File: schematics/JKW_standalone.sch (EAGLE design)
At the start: 165 parts, among them IC1 4093D, IC2 AT-MEGA-8, IC4 ATMEGA2560-16AU, T1 Farnell: 1299313, T2 Farnell: 1299313, T3 Farnell: 1299313, T4 T-IRLMS6702, T5 Farnell: 1299313

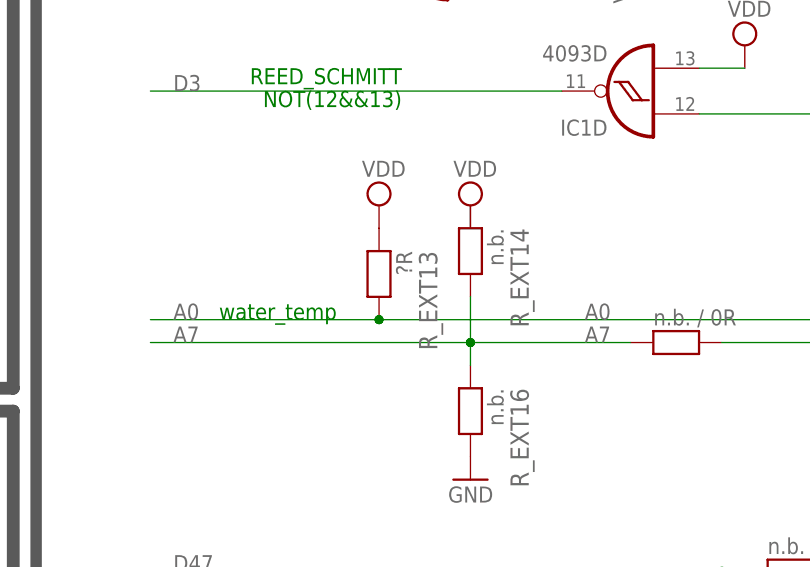
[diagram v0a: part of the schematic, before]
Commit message: Water compare resistor added
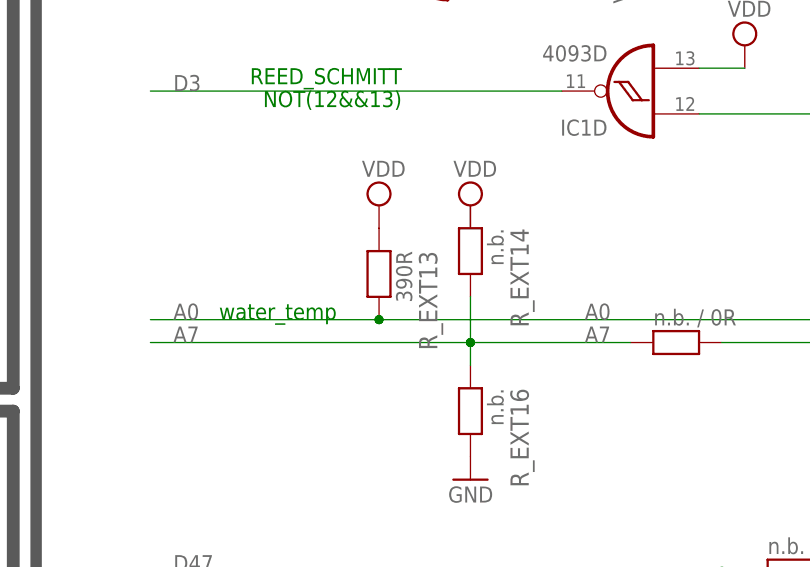
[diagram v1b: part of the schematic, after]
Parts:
- R_EXT13: value ?R -> 390R
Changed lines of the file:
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@@
 <part name="SUPPLY12" library="supply2" deviceset="VDD" device=""/>
 <part name="SUPPLY16" library="supply2" deviceset="VDD" device=""/>
-<part name="R_EXT13" library="RCLDT" deviceset="R" device="0805" value="?R"/>
+<part name="R_EXT13" library="RCLDT" deviceset="R" device="0805" value="390R"/>
 <part name="R_EXT14" library="RCLDT" deviceset="R" device="0805" value="n.b."/>
 <part name="R_EXT16" library="RCLDT" deviceset="R" device="0805" value="n.b."/>

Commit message: New plug
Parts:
- removed ST3, ST4: (no value), Stift+Buchsenleisten:BU_1X4_BL17-SMD
- D7: value SS24 -> n.b. / 20V-ZD.; device RCLDT:D-SSMB-A+K -> diode:ZENER-DIODESOD80C
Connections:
- removed net A10: IC4.PK2(ADC10/PCINT18)
- removed net D20: IC4.(SDA/INT1)PD1, R_SDA_UP.2, ST3.2
- removed net D21: IC4.(SCL/INT0)PD0, R_SCL_UP.2, ST3.3
- removed net EXT_3.3V: C9.1, R_TEMP_ALERT.2, ST4.4, TMP102AIDRLT.ADD0, TMP102AIDRLT.VCC
- removed net EXT_GND: C9.2, ST4.1, TMP102AIDRLT.GND
- removed net EXT_SCL: ST4.2, TMP102AIDRLT.SCL
- removed net EXT_SDA: ST4.3, TMP102AIDRLT.SDA
- new net SCL: IC4.(SCL/INT0)PD0, R_SCL_UP.2, TMP102AIDRLT.SCL
- new net SDA: IC4.(SDA/INT1)PD1, R_SDA_UP.2, TMP102AIDRLT.SDA
- net +3V3_EXT: now also C9.1, R_TEMP_ALERT.2, TMP102AIDRLT.ADD0, TMP102AIDRLT.VCC; no longer ST3.1
- net GND: now also C9.2, TMP102AIDRLT.GND; no longer ST3.4
- net KUPPLUNG_IN: now also D7.C; no longer D7.K
- net V_BAK: now also IC4.PK2(ADC10/PCINT18)
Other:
- note added: "GPS Bat (A10)"

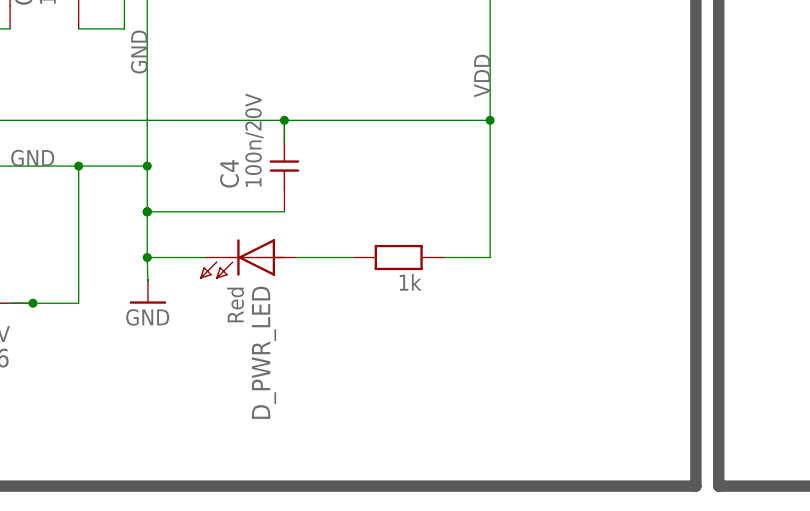
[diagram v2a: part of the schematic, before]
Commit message: GPS surrounded by GND
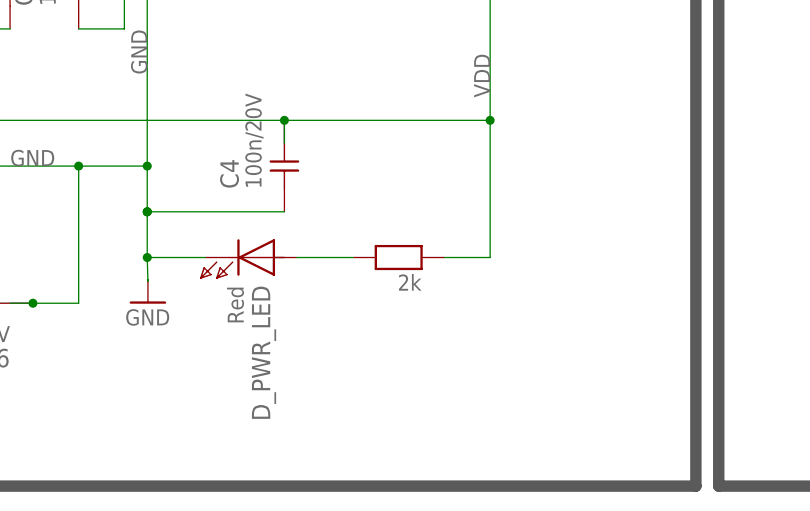
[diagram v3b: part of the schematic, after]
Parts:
- R_LED_5V: value 1k -> 2k
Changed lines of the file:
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@@
 <part name="R38" library="RCLDT" deviceset="R" device="0805" value="n.b."/>
 <part name="R39" library="RCLDT" deviceset="R" device="0805" value="n.b."/>
-<part name="R_LED_5V" library="RCLDT" deviceset="R" device="0805" value="1k"/>
+<part name="R_LED_5V" library="RCLDT" deviceset="R" device="0805" value="2k"/>
 <part name="R_SCL_UP" library="RCLDT" deviceset="R" device="0805" value="1K"/>
 <part name="R_SDA_UP" library="RCLDT" deviceset="R" device="0805" value="1K"/>

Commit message: added 3V emergency voltage
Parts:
- added D13, D14: (no value), semicon-smd-ipc:D-A1-C3
- added D15: Mouser 863-NSR1020MW2T3G, diode:DIODE-SOD323-W
- added D16: n.b. / 20V-ZD., diode:ZENER-DIODESOT23
- D1, D2, D6, D8: device diode:ZENER-DIODESOD80C -> diode:ZENER-DIODESOT23
- D18, D19: value n.b. / 20V-ZD. -> 78-MMBZ5232B-V; device diode:ZENER-DIODESOD80C -> diode:ZENER-DIODESOT23
- D7: value n.b. / 20V-ZD. -> 771-PMBD7000235; device diode:ZENER-DIODESOD80C -> semicon-smd-ipc:D-A1-C3
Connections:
- removed net V_BAK: BAT_CLIP1.+, C7.1, GPS.VBACKUP, IC4.PK2(ADC10/PCINT18)
- new net A10: C7.1, D14.C, D15.C, GPS.VBACKUP, IC4.PK2(ADC10/PCINT18)
- new net N$11: BAT_CLIP1.+, D15.A
- new net N$47: D13.C, D14.A
- net D24: now also D13.A
- net D48: now also D16.C
- net GND: now also D16.A
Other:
- note added: "GPS_V_BACKUP"
- moved on the sheet: C7
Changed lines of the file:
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@@
 <part name="GND9" library="SparkFun" deviceset="GND" device=""/>
 <part name="DCDC53.3" library="Kolja" deviceset="AP1117E33G" device=""/>
-<part name="D6" library="diode" deviceset="ZENER-DIODE" device="SOD80C" value="20V-Zdiode"/>
+<part name="D6" library="diode" deviceset="ZENER-DIODE" device="SOT23" value="20V-Zdiode"/>
 <part name="GND12" library="SparkFun" deviceset="GND" device=""/>
 <part name="GND14" library="SparkFun" deviceset="GND" device=""/>
@@
 <part name="D17" library="RCLDT" deviceset="D-S" device="SMB-A+K" value="SS24"/>
 <part name="12V_F1" library="Kolja" deviceset="POLY_FUSE" device="" value="1.1A"/>
-<part name="D18" library="diode" deviceset="ZENER-DIODE" device="SOD80C" value="n.b. / 20V-ZD."/>
-<part name="D19" library="diode" deviceset="ZENER-DIODE" device="SOD80C" value="n.b. / 20V-ZD."/>
+<part name="D18" library="diode" deviceset="ZENER-DIODE" device="SOT23" value="78-MMBZ5232B-V"/>
+<part name="D19" library="diode" deviceset="ZENER-DIODE" device="SOT23" value="78-MMBZ5232B-V"/>
 <part name="GND6" library="supply1" deviceset="GND" device=""/>
 <part name="GND15" library="supply1" deviceset="GND" device=""/>
@@
 <part name="R_EXT12" library="RCLDT" deviceset="R" device="0805" value="5k"/>
 <part name="GND17" library="supply1" deviceset="GND" device=""/>
-<part name="D1" library="diode" deviceset="ZENER-DIODE" device="SOD80C" value="5.5V"/>
-<part name="D2" library="diode" deviceset="ZENER-DIODE" device="SOD80C" value="5.5V"/>
-<part name="D8" library="diode" deviceset="ZENER-DIODE" device="SOD80C" value="5.5V"/>
+<part name="D1" library="diode" deviceset="ZENER-DIODE" device="SOT23" value="5.5V"/>
+<part name="D2" library="diode" deviceset="ZENER-DIODE" device="SOT23" value="5.5V"/>
+<part name="D8" library="diode" deviceset="ZENER-DIODE" device="SOT23" value="5.5V"/>
 <part name="D9" library="diode" deviceset="ZENER-DIODE" device="SOD80C" value="5.5V"/>
 <part name="D12" library="diode" deviceset="ZENER-DIODE" device="SOD80C" value="20V"/>
@@
 <part name="SUPPLY8" library="supply2" deviceset="VDD" device=""/>
 <part name="SUPPLY19" library="supply2" deviceset="VDD" device=""/>
-<part name="D7" library="diode" deviceset="ZENER-DIODE" device="SOD80C" value="n.b. / 20V-ZD."/>
+<part name="D7" library="semicon-smd-ipc" deviceset="D-" device="A1-C3" value="771-PMBD7000235"/>
+<part name="D13" library="semicon-smd-ipc" deviceset="D-" device="A1-C3"/>
+<part name="D14" library="semicon-smd-ipc" deviceset="D-" device="A1-C3"/>
+<part name="D15" library="diode" deviceset="DIODE-" device="SOD323-W" value="Mouser 863-NSR1020MW2T3G"/>
+<part name="D16" library="diode" deviceset="ZENER-DIODE" device="SOT23" value="n.b. / 20V-ZD."/>
+<part name="U$2" library="SUPPLY" deviceset="GND" device=""/>
 </parts>
 <sheets>
@@
 <text x="35.56" y="139.7" size="1.778" layer="91">water_temp</text>
 <text x="-266.7" y="139.7" size="1.778" layer="91">GPS Bat (A10)</text>
+<text x="-142.24" y="226.06" size="1.778" layer="91">GPS_V_BACKUP</text>
 </plain>
 <instances>
@@
 <attribute name="VALUE" x="271.78" y="106.68" size="1.778" layer="96"/>
 </instance>
-<instance part="C7" gate="C" x="236.22" y="86.36"/>
+<instance part="C7" gate="C" x="236.22" y="93.98"/>
 <instance part="D_GPS_FIX" gate="G$1" x="279.4" y="86.36" smashed="yes" rot="R90">
 <attribute name="NAME" x="277.4061" y="89.0016" size="1.6764" layer="95"/>
@@
 <attribute name="VALUE" x="137.922" y="169.291" size="1.778" layer="96"/>
 </instance>
+<instance part="D13" gate="G$1" x="254" y="119.38"/>
+<instance part="D14" gate="G$1" x="261.62" y="119.38"/>
+<instance part="D15" gate="G$1" x="231.14" y="86.36" rot="R90"/>
+<instance part="D16" gate="G$1" x="127" y="172.72" smashed="yes" rot="R90">
+<attribute name="NAME" x="125.095" y="170.942" size="1.778" layer="95" rot="R90"/>
+<attribute name="VALUE" x="130.429" y="160.782" size="1.778" layer="96" rot="R90"/>
+</instance>
+<instance part="U$2" gate="G$1" x="127" y="165.1"/>
 </instances>
 <busses>
@@
 <wire x1="287.02" y1="83.82" x2="254" y2="83.82" width="0.1524" layer="91"/>
 <wire x1="254" y1="83.82" x2="241.3" y2="83.82" width="0.1524" layer="91"/>
-<wire x1="241.3" y1="83.82" x2="241.3" y2="86.36" width="0.1524" layer="91"/>
-<wire x1="241.3" y1="86.36" x2="241.3" y2="104.14" width="0.1524" layer="91"/>
+<wire x1="241.3" y1="83.82" x2="241.3" y2="93.98" width="0.1524" layer="91"/>
+<wire x1="241.3" y1="93.98" x2="241.3" y2="104.14" width="0.1524" layer="91"/>
 <wire x1="241.3" y1="78.74" x2="241.3" y2="83.82" width="0.1524" layer="91"/>
 <wire x1="287.02" y1="83.82" x2="287.02" y2="86.36" width="0.1524" layer="91"/>
@@
 <junction x="241.3" y="83.82"/>
 <junction x="269.24" y="104.14"/>
-<junction x="241.3" y="86.36"/>
+<junction x="241.3" y="93.98"/>
 <junction x="287.02" y="83.82"/>
 <junction x="254" y="73.66"/>
@@
 <wire x1="289.24" y1="228.6" x2="294.32" y2="228.6" width="0.1524" layer="91"/>
 </segment>
+<segment>
+<pinref part="D16" gate="G$1" pin="A"/>
+<pinref part="U$2" gate="G$1" pin="GND"/>
+<wire x1="127" y1="170.18" x2="127" y2="167.64" width="0.1524" layer="91"/>
+</segment>
 </net>
 <net name="DZ" class="0">
@@
 <segment>
 <pinref part="U$1" gate="G$1" pin="MC_COI"/>
-<wire x1="185.42" y1="177.8" x2="132.08" y2="177.8" width="0.1524" layer="91"/>
+<wire x1="185.42" y1="177.8" x2="127" y2="177.8" width="0.1524" layer="91"/>
 <label x="139.7" y="177.8" size="1.778" layer="95"/>
+<pinref part="D16" gate="G$1" pin="C"/>
+<wire x1="127" y1="177.8" x2="119.38" y2="177.8" width="0.1524" layer="91"/>
+<wire x1="127" y1="175.26" x2="127" y2="177.8" width="0.1524" layer="91"/>
+<junction x="127" y="177.8"/>
 </segment>
 </net>
@@
 <pinref part="IC4" gate="1" pin="(AD2)PA2"/>
 </segment>
+<segment>
+<pinref part="D13" gate="G$1" pin="A"/>
+<wire x1="251.46" y1="119.38" x2="241.3" y2="119.38" width="0.1524" layer="91"/>
+<label x="241.3" y="119.38" size="1.778" layer="95"/>
+</segment>
 </net>
 <net name="D25" class="0">
@@
 </segment>
 </net>
-<net name="V_BAK" class="0">
-<segment>
-<wire x1="231.14" y1="96.52" x2="281.94" y2="96.52" width="0.1524" layer="91"/>
-<wire x1="281.94" y1="96.52" x2="281.94" y2="93.98" width="0.1524" layer="91"/>
-<wire x1="281.94" y1="93.98" x2="292.1" y2="93.98" width="0.1524" layer="91"/>
-<wire x1="231.14" y1="78.74" x2="231.14" y2="86.36" width="0.1524" layer="91"/>
-<wire x1="231.14" y1="86.36" x2="231.14" y2="96.52" width="0.1524" layer="91"/>
-<junction x="231.14" y="86.36"/>
-<label x="246.38" y="83.82" size="1.778" layer="95" rot="R90"/>
-<pinref part="GPS" gate="G$1" pin="VBACKUP"/>
-<pinref part="BAT_CLIP1" gate="G$1" pin="+"/>
-<pinref part="C7" gate="C" pin="1"/>
-</segment>
-<segment>
-<wire x1="-228.6" y1="139.7" x2="-246.38" y2="139.7" width="0.1524" layer="91"/>
-<label x="-243.84" y="139.7" size="1.778" layer="95"/>
-<pinref part="IC4" gate="1" pin="PK2(ADC10/PCINT18)"/>
-</segment>
-</net>
 <net name="N$15" class="0">
 <segment>
@@
 <wire x1="251.46" y1="60.96" x2="251.46" y2="66.04" width="0.1524" layer="91"/>
 <junction x="251.46" y="66.04"/>
-<label x="279.4" y="78.74" size="1.778" layer="95"/>
+<label x="269.24" y="78.74" size="1.778" layer="95"/>
 <pinref part="GPS" gate="G$1" pin="RXD"/>
 <pinref part="R40" gate="G$1" pin="1"/>
@@
 </segment>
 </net>
+<net name="N$47" class="0">
+<segment>
+<pinref part="D14" gate="G$1" pin="A"/>
+<pinref part="D13" gate="G$1" pin="C"/>
+<wire x1="259.08" y1="119.38" x2="256.54" y2="119.38" width="0.1524" layer="91"/>
+</segment>
+</net>
+<net name="A10" class="0">
+<segment>
+<wire x1="-228.6" y1="139.7" x2="-246.38" y2="139.7" width="0.1524" layer="91"/>
+<label x="-233.68" y="139.7" size="1.778" layer="95"/>
+<pinref part="IC4" gate="1" pin="PK2(ADC10/PCINT18)"/>
+</segment>
+<segment>
+<pinref part="GPS" gate="G$1" pin="VBACKUP"/>
+<wire x1="281.94" y1="96.52" x2="281.94" y2="93.98" width="0.1524" layer="91"/>
+<wire x1="281.94" y1="93.98" x2="292.1" y2="93.98" width="0.1524" layer="91"/>
+<wire x1="266.7" y1="96.52" x2="281.94" y2="96.52" width="0.1524" layer="91"/>
+<wire x1="266.7" y1="96.52" x2="266.7" y2="119.38" width="0.1524" layer="91"/>
+<pinref part="D14" gate="G$1" pin="C"/>
+<wire x1="266.7" y1="119.38" x2="264.16" y2="119.38" width="0.1524" layer="91"/>
+<junction x="266.7" y="119.38"/>
+<wire x1="266.7" y1="119.38" x2="281.94" y2="119.38" width="0.1524" layer="91"/>
+<label x="274.32" y="119.38" size="1.778" layer="95"/>
+<pinref part="C7" gate="C" pin="1"/>
+<wire x1="266.7" y1="96.52" x2="231.14" y2="96.52" width="0.1524" layer="91"/>
+<wire x1="231.14" y1="96.52" x2="231.14" y2="93.98" width="0.1524" layer="91"/>
+<pinref part="D15" gate="G$1" pin="C"/>
+<wire x1="231.14" y1="88.9" x2="231.14" y2="93.98" width="0.1524" layer="91"/>
+<junction x="231.14" y="93.98"/>
+</segment>
+</net>
+<net name="N$11" class="0">
+<segment>
+<pinref part="D15" gate="G$1" pin="A"/>
+<pinref part="BAT_CLIP1" gate="G$1" pin="+"/>
+<wire x1="231.14" y1="83.82" x2="231.14" y2="78.74" width="0.1524" layer="91"/>
+</segment>
+</net>

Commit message: GPS schematic updated
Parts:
- removed R28: 1k, RCLDT:R0805
- removed R40: 2k7, RCLDT:R0805
- removed R41: 1k2, RCLDT:R0805
- removed R_OIL_V_DIV_2: 220, RCLDT:R0805
- added D20: 5.5V, diode:ZENER-DIODESOT23
- added R_GPS_LED: 1k, RCLDT:R0805
- added R_OIL_UP: 220, RCLDT:R0805
- added R_TX_DOWN: 2k7, RCLDT:R0805
- added R_TX_UP: 1k2, RCLDT:R0805
- S6: value U -> Left
- S7: value R -> Down
- S8: value D -> Up
- S9: value L -> Right
- renumbered 18632422 to RGB_3, D10 to D_L1, D11 to D_L2, D3 to D_L0, R1 to R_BL_L, R10 to R_REED_DOWN, R11 to R_REED, R12 to R_R_LED_3, R13 to R_G_LED_3, R14 to R_B_LED_3, R15 to R_L0, R16 to R_L1, R17 to R_L2, R18 to R_R_LED_2, R19 to R_G_LED_2, R2 to R_RES_UP, R20 to R_B_LED_2, R21 to R_R_LED_1, R22 to R_G_LED_1, R23 to R_B_LED_1, R24 to R_R_LED_0, R25 to R_G_LED_0, R26 to R_B_LED_0, R27 to R_N, R29 to R_R_LED_4, R3 to AT8_REF, R30 to R_G_LED_4, R31 to R_B_LED_4, R32 to R_R_LED_5, R33 to R_G_LED_5, R34 to R_B_LED_5, R35 to R_R_LED_6, R36 to R_G_LED_6, R37 to R_B_LED_6, R38 to R_E1_4, R39 to R_E1_2, R4 to R_BL_R, R43 to R_E2_1, R44 to R_E1_3, R45 to R_E0_0, R46 to R_E0_1, R47 to R_E0_3, R48 to R_E0_4, R49 to R_E0_2, R5 to R_OIL, R6 to R_HIGHB, R7 to R_REED_UP, R8 to R_E1_0, R9 to R_E1_1, R_DZ_DIV1 to R_DZ, R_DZ_DIV2 to R_DZ_DOWN, R_EXT10 to R_FLASHR, R_EXT11 to R_HB, R_EXT12 to R_HB_DOWN, R_EXT13 to R_WATER_UP, R_EXT14 to R_E2_0, R_EXT16 to R_E2_2, R_EXT7 to R_FLASHL, R_EXT8 to R_FLASHL_DOWN, R_EXT9 to R_FLASHR_DOWN, U$14 to RGB_7, U$15 to RGB_4, U$16 to RGB_6, U$18 to RGB_5, U$19 to RGB_2, U$20 to RGB_1
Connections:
- net B_D renamed B_UP
- net B_L renamed B_RIGHT
- net B_R renamed B_DOWN
- net B_U renamed B_LEFT
- net D35 renamed DISP_SCL
- net A1: now also D20.C, R_OIL_UP.1; no longer R_OIL_V_DIV_2.1
- net GND: now also D20.A, R_TX_DOWN.2; no longer R40.2
- net N$15: now also R_GPS_LED.2; no longer R28.2
- net N$17: now also R_GPS_LED.1; no longer R28.1
- net TX1: now also R_TX_UP.2; no longer R41.2
- net TX1_3.3: now also R_TX_DOWN.1, R_TX_UP.1; no longer R40.1, R41.1
- net VDD: now also R_OIL_UP.2; no longer R_OIL_V_DIV_2.2
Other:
- note removed: "Floatet das? Warum ist da kein Pullup?"
- note removed: "SpeedSensor"
- note removed: "down"
- note removed: "left"
- note removed: "right"
- note removed: "up"
- moved on the sheet: BAT_CLIP1, C5, C7, D13, D14, D15, D9, D_GPS_FIX, R_V_HIGH, R_V_LOW, S6, S7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

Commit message: Changed to push buttons with plate
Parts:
- removed C38: 2µ2/100V, RCLDT:C0805
- removed C46: 470µ, RCLDT:C-ELKO-5-8X13R
- removed C49: 470µ, RCLDT:C-ELKO-5-8X13
- removed S6: Left, SWITCH+RELAIS:SW-TASTERECO-DIAGONAL
- removed S7: Down, SWITCH+RELAIS:SW-TASTERECO-DIAGONAL
- removed S8: Up, SWITCH+RELAIS:SW-TASTERECO-DIAGONAL
- removed S9: Right, SWITCH+RELAIS:SW-TASTERECO-DIAGONAL
- added B_DOWN, B_LEFT, B_RIGHT, B_UP: SMD_TASTER_MIT_KAPPE, Kolja:SMD_TASTER_MIT_KAPPE
- added CP1, CP2, CP3, CP4: 220µF/16V, Kolja:C_SMD_SMP
- added D10, D21, D22, D3: 5.5V, diode:ZENER-DIODESOT23
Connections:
- removed net D37: IC4.(A8)PC0
- removed net D40: IC4.(RD)PG1
- removed net D41: IC4.(WR)PG0
- net A0: now also D3.C
- net A7: now also D22.C
- net BAT+: now also CP3.PLUS, CP4.PLUS; no longer C38.2, C49.1
- net B_DOWN: now also B_DOWN.OUT; no longer S7.2
- net B_LEFT: now also B_LEFT.OUT; no longer S6.2
- net B_RIGHT: now also B_RIGHT.OUT; no longer S9.2
- net B_UP: now also B_UP.OUT; no longer S8.2
- net GND: now also B_DOWN.IN, B_LEFT.IN, B_RIGHT.IN, B_UP.IN, CP1.GND, CP2.GND, CP3.GND, CP4.GND, D10.A, D21.A, D22.A, D3.A, IC4.(WR)PG0; no longer C38.1, C46.2, C49.2, S6.1, S7.1, S8.1, S9.1
- net N$1: now also CP1.PLUS, CP2.PLUS; no longer C46.1
- net N$19: now also 5V_F.P$2; no longer 5V_F.P$1
- net NG_IN: now also D10.C
- net OIL_PR_IN: now also D21.C
- net VDD: now also 5V_F.P$1, IC4.(A8)PC0, IC4.(RD)PG1; no longer 5V_F.P$2
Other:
- note added: "210"
- note added: "Adr 0"
- note added: "Adr 1"
- note added: "Adr 2"
- note added: "HW Adr"
- note added: "HW06: 111"
- note added: "HW07: 110"
- note added: "HW08: 101"
- note added: "HW09: 100"
- note added: "HW10: 011"
- note added: "HW11: 010"
- note added: "HW12: 001"
- note added: "HW13: 000"
- note added: "V: 6 + (not(Adr2)<<2 || not(Adr1)<<1 || not(Ard0)<<0 )"
- note removed: "neu"
- moved on the sheet: 16MHZ, 5V_F, C11, C18, C4, C6, C_ATM1, C_ATM2, C_ATMEGA, C_QUA_1, C_QUA_2, C_QUA_3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
